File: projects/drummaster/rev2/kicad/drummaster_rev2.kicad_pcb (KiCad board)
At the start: 2 copper layers, 99.7 x 99.7 mm, 169 parts, among them K1 PINS_5, K2 PINS_5, K3 PINS_4, K4 PINS_5, K5 PINS_6, K6 PINS_4, K7 ENCODER, P1 CONN_2, Q1 MOSFET_P, SW1 PROG, U1 TEENSY_3.1, U10 MCP46X1, U11 MCP46X1, U12 MCP46X1, U13 MCP46X1, U14 MCP46X1, U15 MCP46X1, U16 S25FL512S, U2 MCP6004T, U3 MCP6004T, U4 MCP6004T, U5 MCP6004T, U6 MCP6004T, U7 MCP6004T, U8 74HC4067, U9 74HC4067

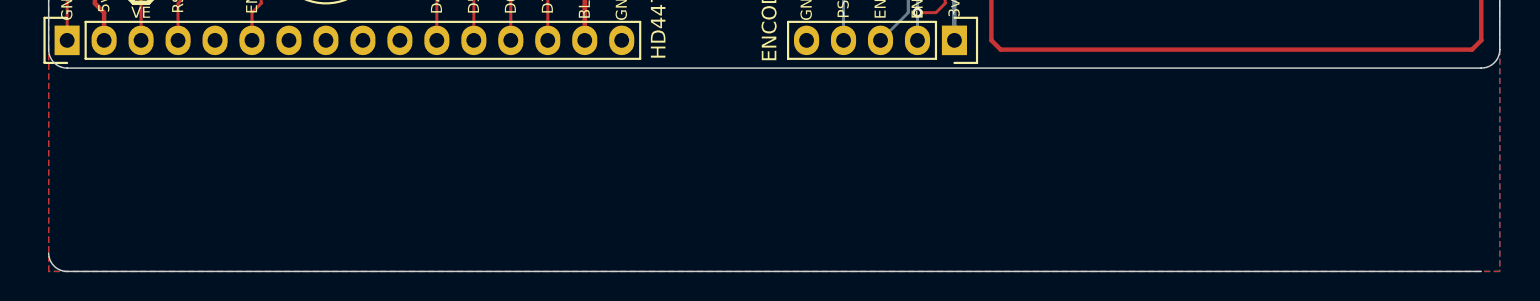
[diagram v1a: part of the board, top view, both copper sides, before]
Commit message: Putting a test motor mount on drummaster board
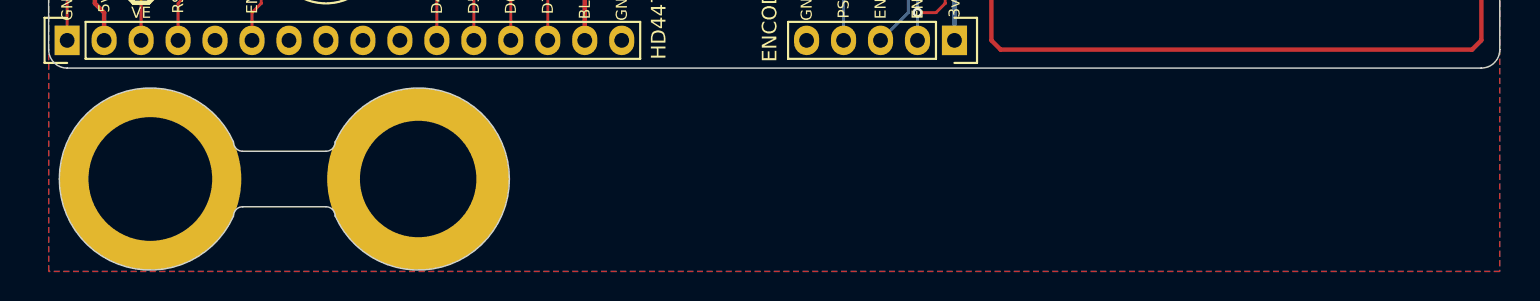
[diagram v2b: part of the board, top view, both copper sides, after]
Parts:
- added REF**: 1pin, Connect:1pin, B.Cu at (81.3, 139.1)
- added REF**: 1pin, Connect:1pin, F.Cu at (62.9, 139.1)
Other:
- board size 99.7 x 99.7 mm -> 99.7 x 99.6 mm
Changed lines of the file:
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@@
     (area 45.340001 40.330001 155.933991 145.465001)
     (thickness 1.6)
-    (drawings 13)
+    (drawings 19)
     (tracks 1731)
     (zones 0)
-    (modules 169)
+    (modules 171)
     (nets 175)
   )
@@
     (mod_text_size 1 1)
     (mod_text_width 0.15)
-    (pad_size 0.8001 1.00076)
-    (pad_drill 0)
+    (pad_size 12.5 12.5)
+    (pad_drill 8)
     (pad_to_mask_clearance 0)
     (aux_axis_origin 0 0)
@@
     (add_net "Net-(U8-Pad19)")
   )
+  (module Connect:1pin (layer B.Cu)
+    (at 81.265503 139.065 180)
+    (descr "module 1 pin (ou trou mecanique de percage)")
+    (tags DEV)
+    (fp_text reference REF** (at 0 3.048 180) (layer B.SilkS) hide
+      (effects (font (size 1 1) (thickness 0.15)) (justify mirror))
+    )
+    (fp_text value 1pin (at 0 -2.794 180) (layer B.Fab) hide
+      (effects (font (size 1 1) (thickness 0.15)) (justify mirror))
+    )
+    (pad 1 thru_hole circle (at 0 0 180) (size 12.5 12.5) (drill 8) (layers *.Cu *.Mask B.SilkS))
+  )
+  (module Connect:1pin (layer F.Cu)
+    (at 62.865 139.065)
+    (descr "module 1 pin (ou trou mecanique de percage)")
+    (tags DEV)
+    (fp_text reference REF** (at 0 -3.048) (layer F.SilkS) hide
+      (effects (font (size 1 1) (thickness 0.15)))
+    )
+    (fp_text value 1pin (at 0 2.794) (layer F.Fab) hide
+      (effects (font (size 1 1) (thickness 0.15)))
+    )
+    (pad 1 thru_hole circle (at 0 0) (size 12.5 12.5) (drill 8.5) (layers *.Cu *.Mask F.SilkS))
+  )
   (module Pin_Headers:Pin_Header_Straight_1x05 (layer F.Cu)
     (at 118.11 129.54 270)
@@
     )
   )
+  (gr_line (start 69.215 140.97) (end 74.93 140.97) (layer Edge.Cuts) (width 0.1))
+  (gr_line (start 74.93 137.16) (end 69.215 137.16) (layer Edge.Cuts) (width 0.1))
+  (gr_arc (start 74.93 136.525) (end 75.565 136.525) (angle 90) (layer Edge.Cuts) (width 0.1))
+  (gr_arc (start 74.93 141.605) (end 74.93 140.97) (angle 90) (layer Edge.Cuts) (width 0.1))
+  (gr_arc (start 81.28 139.065) (end 75.565 136.525) (angle 312.0750221) (layer Edge.Cuts) (width 0.1))
+  (gr_arc (start 69.215 141.605) (end 68.58 141.605) (angle 90) (layer Edge.Cuts) (width 0.1))
+  (gr_arc (start 69.215 136.525) (end 69.215 137.16) (angle 90) (layer Edge.Cuts) (width 0.1))
+  (gr_arc (start 62.865 139.065) (end 68.58 141.605) (angle 312.0750221) (layer Edge.Cuts) (width 0.1))
   (gr_line (start 155.575 46.99) (end 155.575 130.175) (angle 90) (layer Edge.Cuts) (width 0.1))
   (gr_line (start 55.88 130.175) (end 55.88 46.99) (angle 90) (layer Edge.Cuts) (width 0.1))
@@
   (gr_arc (start 57.15 130.175) (end 57.15 131.445) (angle 90) (layer Edge.Cuts) (width 0.1))
   (gr_arc (start 154.305 130.175) (end 155.575 130.175) (angle 90) (layer Edge.Cuts) (width 0.1))
-  (gr_line (start 57.15 145.415) (end 154.305 145.415) (angle 90) (layer Edge.Cuts) (width 0.1))
   (gr_line (start 154.305 45.72) (end 57.15 45.72) (angle 90) (layer Edge.Cuts) (width 0.1))
   (dimension 99.695 (width 0.3) (layer Cmts.User)
@@
     (effects (font (size 1.27 1.27) (thickness 0.3175)))
   )
-  (gr_arc (start 57.15 144.145) (end 57.15 145.415) (angle 90) (layer Edge.Cuts) (width 0.1))
   (gr_arc (start 154.305 46.99) (end 154.305 45.72) (angle 90) (layer Edge.Cuts) (width 0.1))
   (gr_arc (start 57.15 46.99) (end 55.88 46.99) (angle 90) (layer Edge.Cuts) (width 0.1))

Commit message: Changing order of pads to better suit standard drum layout
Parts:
- moved MP3 29.4 mm to (153.0, 117.5)
- moved D7 25.4 mm to (82.5, 55.9)
- moved K4 12.7 mm to (105.4, 49.5)
- moved MP2 11.4 mm to (58.4, 55.2)
- moved K3 10.2 mm to (95.2, 49.5)
- moved MP4 9.55 mm to (153.0, 55.2)
- moved L15 7.65 mm to (145.4, 109.2)
- moved C36 7.62 mm to (141.6, 125.1)
- moved C37 7.62 mm to (142.9, 111.1)
- moved U16 7.62 mm to (140.3, 118.1)
- moved F1 6.84 mm to (144.8, 54.0), turned to 0 degrees
- moved P1 5.68 mm to (146.1, 49.5)
- moved C39 3.24 mm to (60.3, 92.7), turned to 180 degrees
- moved MP1 1.27 mm to (58.4, 117.5)
- renumbered K4 to K3, K3 to K4
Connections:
- net /CX renamed /X1
- net /CX_A renamed /X1_A
- net /CX_D renamed /X1_D
- C10 pad 1: /BS_D -> /SN_D
- C11 pad 1: /T3_D -> /CR_D
- C12 pad 1: /T2_D -> /T1_D
- C13 pad 1: /HP_D -> /T3_D
- C14 pad 1: /HH_D -> /T2_D
- C15 pad 1: /CR_D -> /RD_D
- C18 pad 1: /RD_D -> /X0_D
- C44 pad 2: /SM -> /CM
- C45 pad 2: /CM -> /SM
- C7 pad 1: /SN_D -> /HP_D
- C8 pad 1: /DX_D -> /HH_D
- C9 pad 1: /T1_D -> /BS_D
- D10 pad 2: /DX_D -> /HH_D
- D11 pad 2: /T1_D -> /BS_D
- D12 pad 2: /BS_D -> /SN_D
- D13 pad 2: /T3_D -> /CR_D
- D14 pad 2: /T2_D -> /T1_D
- D15 pad 2: /HP_D -> /T3_D
- D16 pad 2: /HH_D -> /T2_D
- D17 pad 2: /CR_D -> /RD_D
- D20 pad 2: /RD_D -> /X0_D
- D7 pad 1: /SM -> /CM
- D8 pad 2: /CM -> /SM
- D9 pad 2: /SN_D -> /HP_D
- K1 pad 3: /SN -> /HP
- K1 pad 4: /DX -> /HH
- K1 pad 5: GND -> /HM
- K2 pad 3: /T1 -> /BS
- K2 pad 4: /BS -> /SN
- K3 pad 1: /HM -> GND
- K3 pad 2: /HP -> /CM
- K3 pad 3: /HH -> /CR
- K3 pad 4: +3V3 -> /T1
- K5 pad 2: /CM -> /RM
- K5 pad 3: /CR -> /RD
- K6 pad 3: /RD -> /X0
- K6 pad 4: /RM -> GND
- R15 pad 1: /CM -> /SM
- R2 pad 1: /SM -> /CM
- R25 pad 1: /SN -> /HP
- R26 pad 1: /DX -> /HH
- R27 pad 1: /T1 -> /BS
- R28 pad 1: /BS -> /SN
- R29 pad 1: /T3 -> /CR
- R30 pad 1: /T2 -> /T1
- R31 pad 1: /HP -> /T3
- R32 pad 1: /HH -> /T2
- R33 pad 1: /CR -> /RD
- R36 pad 1: /RD -> /X0
- U10 pad 7: /SN_A -> /HP_A
- U10 pad 8: /DX_A -> /HH_A
- U11 pad 7: /T1_A -> /BS_A
- U11 pad 8: /BS_A -> /SN_A
- U12 pad 7: /T3_A -> /CR_A
- U12 pad 8: /T2_A -> /T1_A
- U13 pad 7: /HP_A -> /T3_A
- U13 pad 8: /HH_A -> /T2_A
- U14 pad 7: /CR_A -> /RD_A
- U15 pad 8: /RD_A -> /X0_A
- U2 pad 1: /DX_A -> /HH_A
- U2 pad 13: /DX_D -> /HH_D
- U2 pad 3: /DX_D -> /HH_D
- U2 pad 5: /SN_D -> /HP_D
- U2 pad 7: /SN_A -> /HP_A
- U2 pad 9: /SN_D -> /HP_D
- U3 pad 1: /BS_A -> /SN_A
- U3 pad 13: /BS_D -> /SN_D
- U3 pad 3: /BS_D -> /SN_D
- U3 pad 5: /T1_D -> /BS_D
- U3 pad 7: /T1_A -> /BS_A
- U3 pad 9: /T1_D -> /BS_D
- U4 pad 1: /T2_A -> /T1_A
- U4 pad 13: /T2_D -> /T1_D
- U4 pad 3: /T2_D -> /T1_D
- U4 pad 5: /T3_D -> /CR_D
- U4 pad 7: /T3_A -> /CR_A
- U4 pad 9: /T3_D -> /CR_D
- U5 pad 1: /HH_A -> /T2_A
- U5 pad 13: /HH_D -> /T2_D
- U5 pad 3: /HH_D -> /T2_D
- U5 pad 5: /HP_D -> /T3_D
- U5 pad 7: /HP_A -> /T3_A
- U5 pad 9: /HP_D -> /T3_D
- U6 pad 5: /CR_D -> /RD_D
- U6 pad 7: /CR_A -> /RD_A
- U6 pad 9: /CR_D -> /RD_D
- U7 pad 1: /RD_A -> /X0_A
- U7 pad 13: /RD_D -> /X0_D
- U7 pad 3: /RD_D -> /X0_D
- U8 pad 2: /HP_D -> /T3_D
- U8 pad 21: /RD_D -> /X0_D
- U8 pad 22: /CR_D -> /RD_D
- U8 pad 3: /HH_D -> /T2_D
- U8 pad 4: /T3_D -> /CR_D
- U8 pad 5: /T2_D -> /T1_D
- U8 pad 6: /T1_D -> /BS_D
- U8 pad 7: /BS_D -> /SN_D
- U8 pad 8: /SN_D -> /HP_D
- U8 pad 9: /DX_D -> /HH_D
- U9 pad 17: /SM -> /CM
- U9 pad 18: /CM -> /SM
- U9 pad 2: /HP_A -> /T3_A
- U9 pad 21: /RD_A -> /X0_A
- U9 pad 22: /CR_A -> /RD_A
- U9 pad 3: /HH_A -> /T2_A
- U9 pad 4: /T3_A -> /CR_A
- U9 pad 5: /T2_A -> /T1_A
- U9 pad 6: /T1_A -> /BS_A
- U9 pad 7: /BS_A -> /SN_A
- U9 pad 8: /SN_A -> /HP_A
- U9 pad 9: /DX_A -> /HH_A
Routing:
- net /DX_D: track 102.7 -> 0.00 mm, vias 2 -> 0
- net /DX_A: track 91.1 -> 0.00 mm
- net /X0_D: track 0.00 -> 68.1 mm, vias 0 -> 2
- net /HM: track 92.1 -> 157.8 mm
- net /HH_A: track 49.2 -> 91.1 mm
- net /HP_A: track 37.1 -> 79.0 mm
- net /X0_A: track 0.00 -> 39.9 mm
- net /HP_D: track 60.2 -> 99.9 mm
- net /HH_D: track 63.0 -> 102.7 mm
- net /CM: track 76.3 -> 110.6 mm
- net +3V3: track 536.5 -> 517.8 mm
- net /SCLK: track 83.9 -> 66.4 mm
- net /MOSI: track 77.6 -> 61.4 mm
- net /T2_A: track 63.1 -> 49.2 mm
- net /T3_A: track 51.0 -> 37.1 mm
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
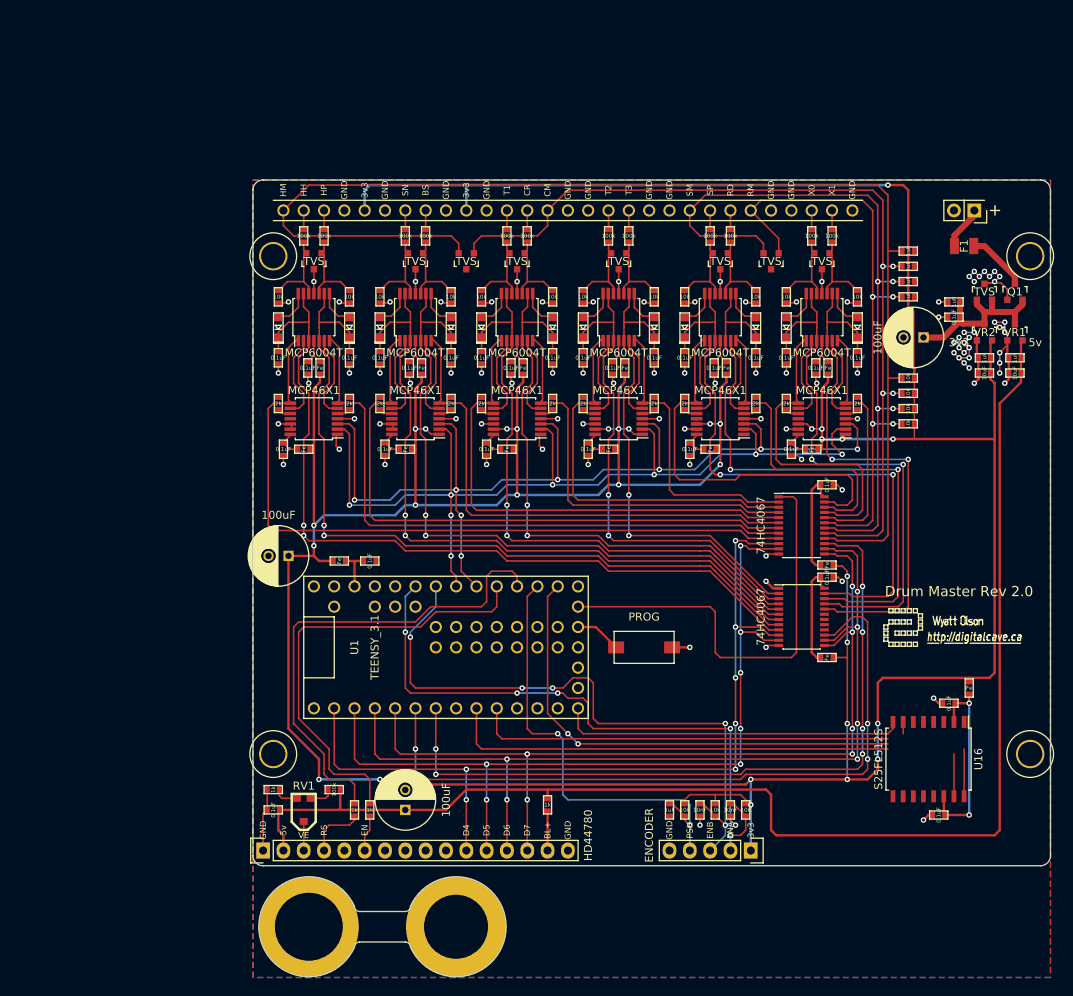
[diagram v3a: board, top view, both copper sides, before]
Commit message: Updated schematic and board to most recent breadboard version
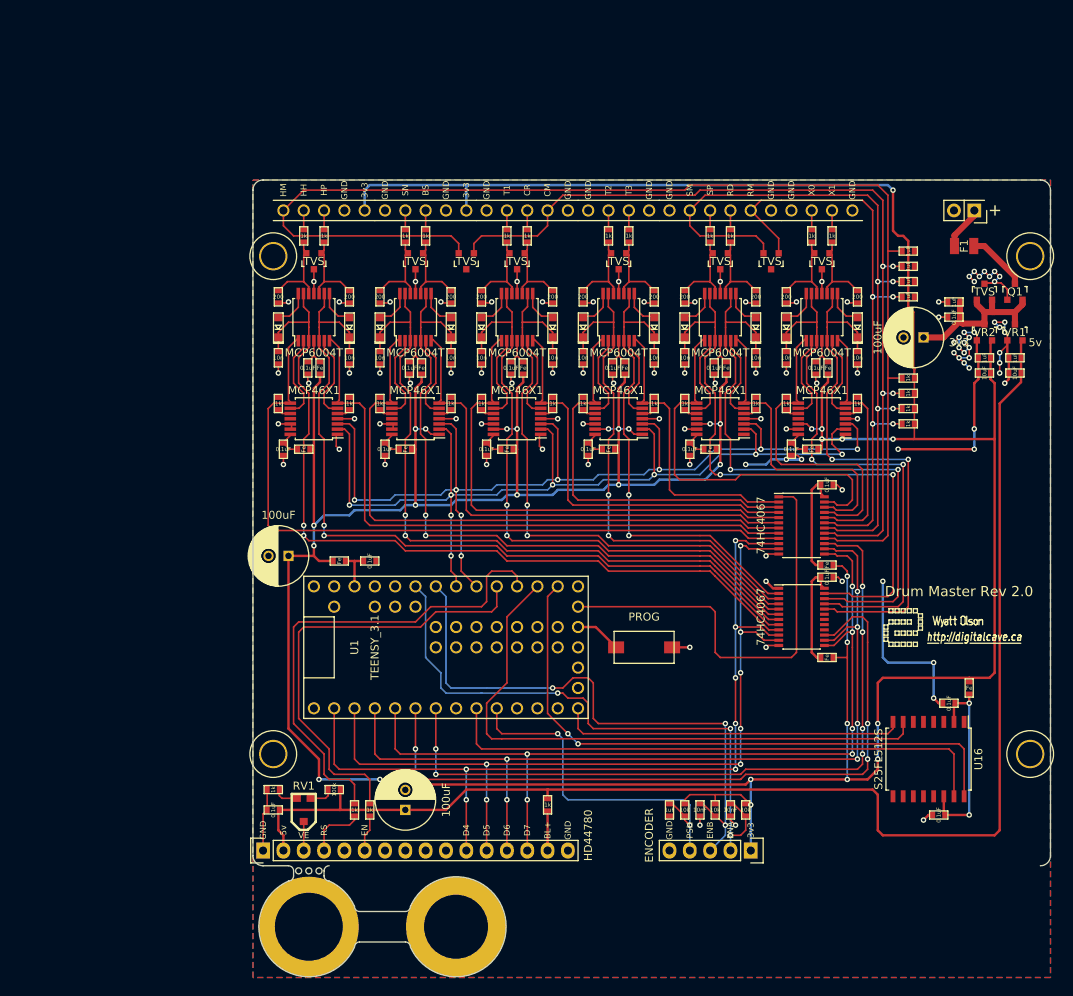
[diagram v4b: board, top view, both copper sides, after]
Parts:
- added mouse_bites: VAL**, DigitalCave:mouse_bites, F.Cu at (62.9, 132.1)
- C10, C11, C12, C13, C14, C15, C16, C17, C18, C7, C8, C9: value 0.1uF -> 10n
- R1, R15, R16, R2: value 10k -> 1k
- R10, R11, R12, R13, R14, R3, R4, R5, R6, R7, R8, R9: value 10k -> 200
- R25, R26, R27, R28, R29, R30, R31, R32, R33, R34, R35, R36: value 100k -> 1k
- R37, R38, R39, R40, R41, R42, R43, R44, R45, R46, R47, R48: value 2k -> 1k
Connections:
- U1 pad 15: /ENC_PUSH -> /MEM2CS
- U1 pad 8: /MEM2CS -> /ENC_PUSH
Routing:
- net GND: track 164.5 -> 212.0 mm, vias 100 -> 106
- net /MEM2CS: track 53.8 -> 75.1 mm
- net /ENC_PUSH: track 56.3 -> 44.4 mm
- net /SCLK: track 66.4 -> 76.2 mm
- net /MOSI: track 61.4 -> 69.9 mm
- net /ENC_B: track 79.5 -> 74.2 mm, vias 5 -> 3
- net /ENC_A: track 79.2 -> 75.5 mm, vias 5 -> 3
- net +3V3: track 517.8 -> 517.0 mm
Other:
- outline, holes or cut-outs redrawn

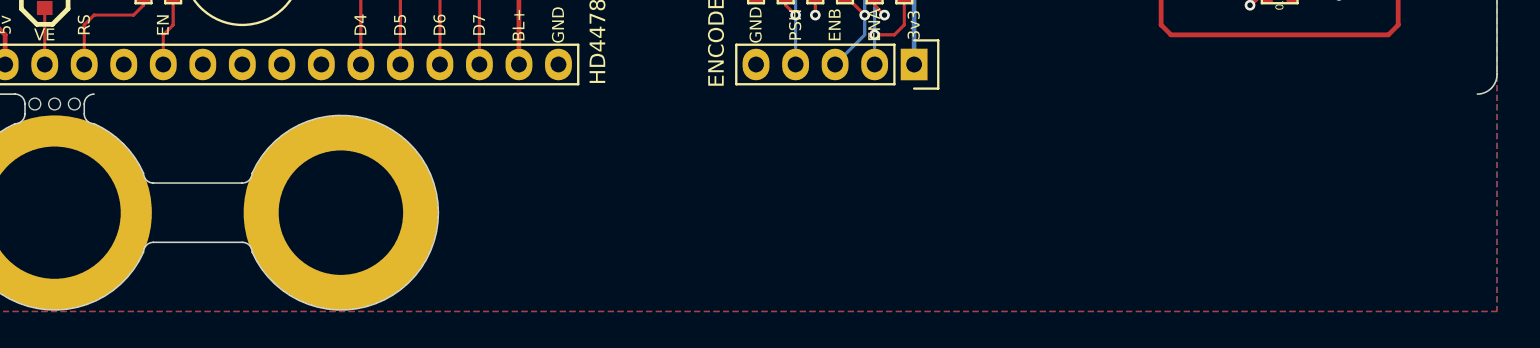
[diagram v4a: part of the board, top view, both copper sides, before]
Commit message: Added some breakout boards to the drummaster PCB
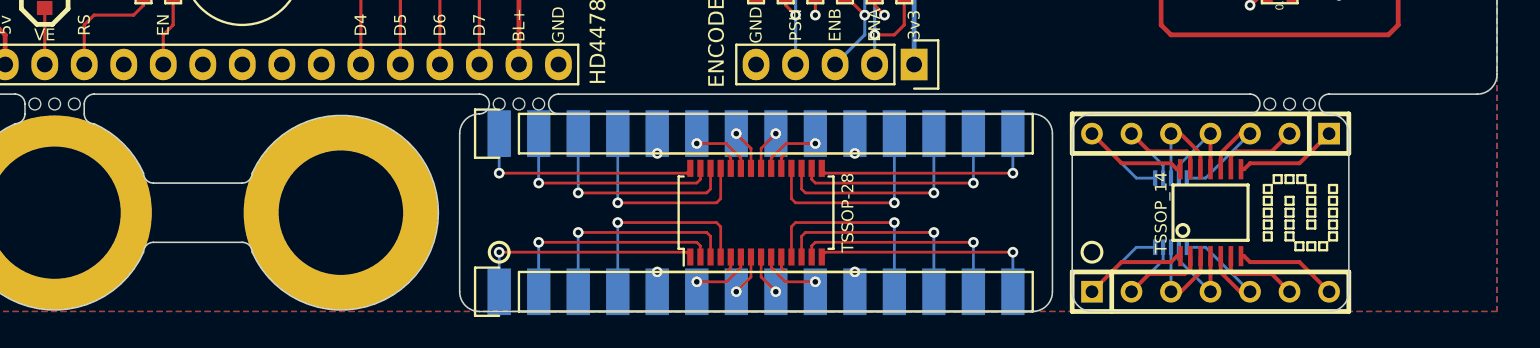
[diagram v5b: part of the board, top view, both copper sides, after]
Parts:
- added K1: TSSOP-28, Housings_SSOP:TSSOP-28_4.4x9.7mm_Pitch0.65mm, F.Cu at (108.0, 139.1)
- added K1: PINS_7, SIL-7, F.Cu at (137.2, 144.1)
- added K2: DIP, Pin_Headers:Pin_Header_Straight_1x14, F.Cu at (91.4, 144.1)
- added K2: PINS_7, SIL-7, F.Cu at (137.2, 134.0)
- added K3: DIP, Pin_Headers:Pin_Header_Straight_1x14, F.Cu at (91.4, 134.0)
- added K3: MSSOP_10, MSOP10-0.5, B.Cu at (134.6, 139.1)
- added K4: TSSOP_14, TSSOP14, F.Cu at (137.2, 139.1)
- added VAL: REF, DIGITALCAVE_LOGO, F.Cu at (142.9, 139.1)
- added VAL: REF, DIGITALCAVE_LOGO, B.Cu at (142.9, 139.1)
- added mouse_bites: VAL**, DigitalCave:mouse_bites, F.Cu at (142.2, 132.1)
- added mouse_bites: VAL**, DigitalCave:mouse_bites, F.Cu at (92.7, 132.1)
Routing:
- net Net-(K1-Pad14): track 0.00 -> 15.0 mm, vias 0 -> 1
- net Net-(K1-Pad1): track 0.00 -> 15.0 mm, vias 0 -> 1
- net Net-(K1-Pad28): track 0.00 -> 15.0 mm, vias 0 -> 1
- net Net-(K1-Pad15): track 0.00 -> 15.0 mm, vias 0 -> 1
- net Net-(K1-Pad2): track 0.00 -> 14.4 mm, vias 0 -> 1
- net Net-(K1-Pad13): track 0.00 -> 14.4 mm, vias 0 -> 1
- net Net-(K1-Pad27): track 0.00 -> 14.4 mm, vias 0 -> 1
- net Net-(K1-Pad16): track 0.00 -> 14.4 mm, vias 0 -> 1
- net Net-(K1-Pad3): track 0.00 -> 13.7 mm, vias 0 -> 1
- net Net-(K1-Pad12): track 0.00 -> 13.7 mm, vias 0 -> 1
- net Net-(K1-Pad26): track 0.00 -> 13.7 mm, vias 0 -> 1
- net Net-(K1-Pad17): track 0.00 -> 13.7 mm, vias 0 -> 1
- net Net-(K1-Pad11): track 0.00 -> 13.4 mm, vias 0 -> 1
- net Net-(K1-Pad25): track 0.00 -> 13.4 mm, vias 0 -> 1
- net Net-(K1-Pad4): track 0.00 -> 13.1 mm, vias 0 -> 1
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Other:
- board size 99.7 x 99.6 mm -> 99.7 x 99.7 mm
- net class Default: trace_width 0.2032 -> 0.1778; via_dia 0.6858 -> 0.889; via_drill 0.3556 -> 0.635
- rule via_min_drill: 0.3556 -> 0.508
- rule via_min_size: 0.3556 -> 0.889
